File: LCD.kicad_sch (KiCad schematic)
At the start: 9 parts, among them J1 AFC01-S40FCA-00, J2 AFC07-S10ECC-00

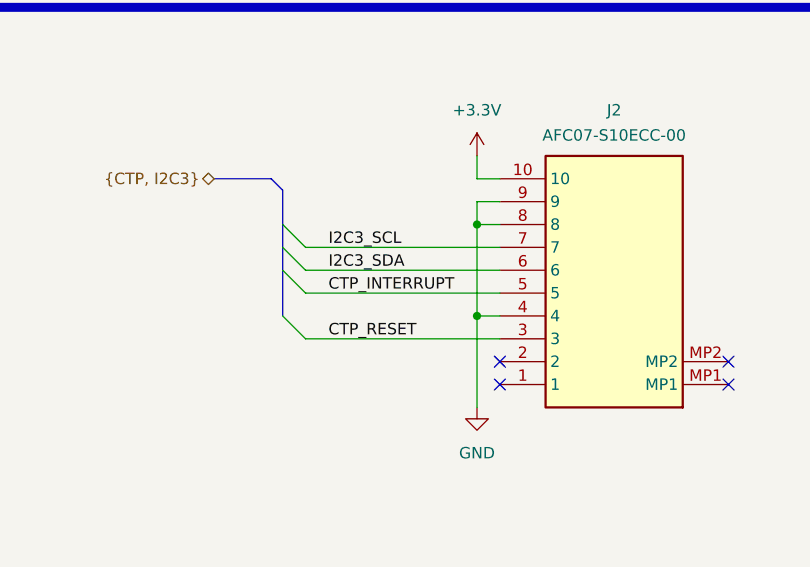
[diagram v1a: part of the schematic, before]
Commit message: added RF ransceiver
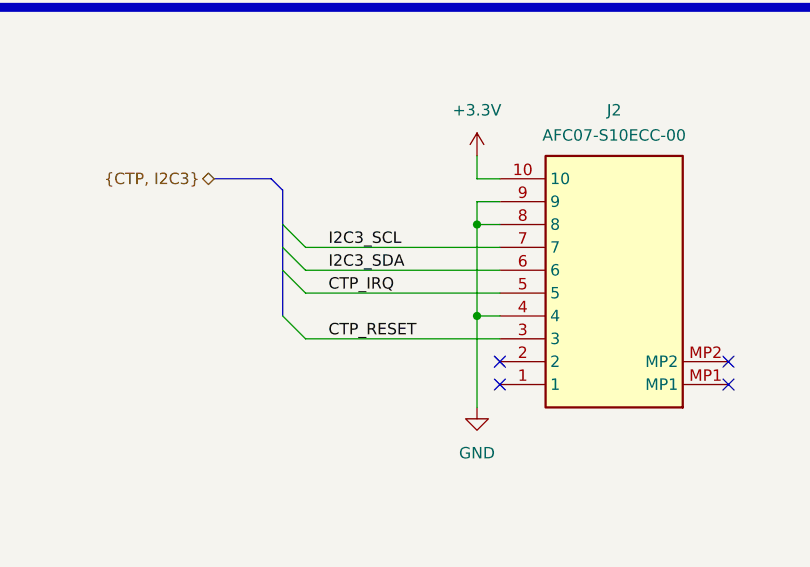
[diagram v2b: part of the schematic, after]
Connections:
- net CTP_INTERRUPT: no longer J2.5
- new net CTP_IRQ: J2.5
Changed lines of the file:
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@@
 	)
 	(bus_alias "CTP"
-		(members "CTP_INTERRUPT" "CTP_RESET")
+		(members "CTP_IRQ" "CTP_RESET")
 	)
 	(bus_alias "LCD_BACKLIGHT"
@@
 		)
 	)
-	(label "CTP_INTERRUPT"
+	(label "CTP_IRQ"
 		(at 227.33 198.12 0)
 		(effects

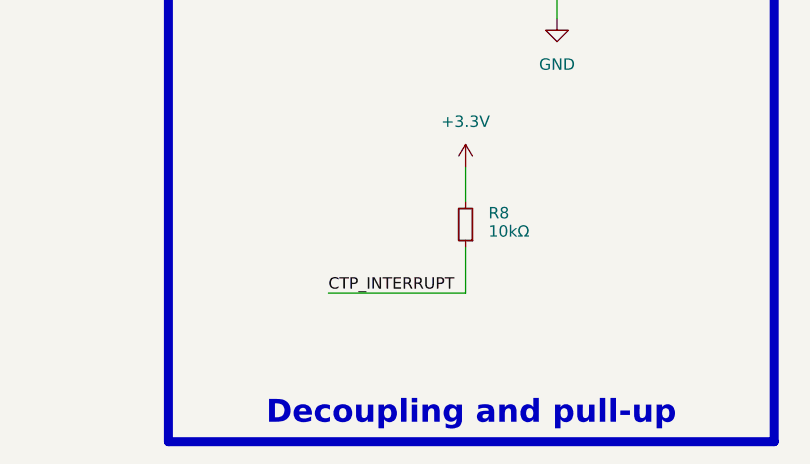
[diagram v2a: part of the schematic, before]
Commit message: added auxialry - swd connector and NRST pin circuit
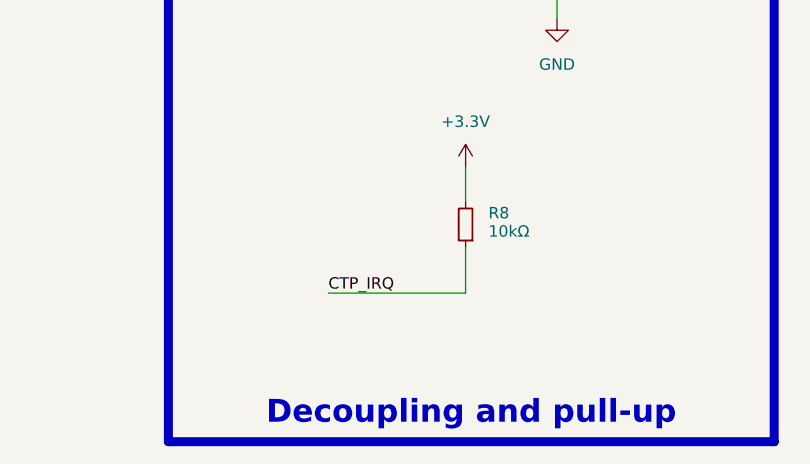
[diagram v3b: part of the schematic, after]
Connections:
- net CTP_INTERRUPT is gone; now on net CTP_IRQ: R8.1
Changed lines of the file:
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@@
-		)
-	)
-	(label "CTP_INTERRUPT"
-		(at 119.38 224.79 0)
-		(effects
-			(font
-				(size 1.27 1.27)
-			)
-			(justify left bottom)
 		)
 	)
@@
 		(effects
 			(font
+				(size 1.27 1.27)
+			)
+			(justify left bottom)
+		)
+	)
+	(label "CTP_IRQ"
+		(at 119.38 224.79 0)
+		(effects
+			(font

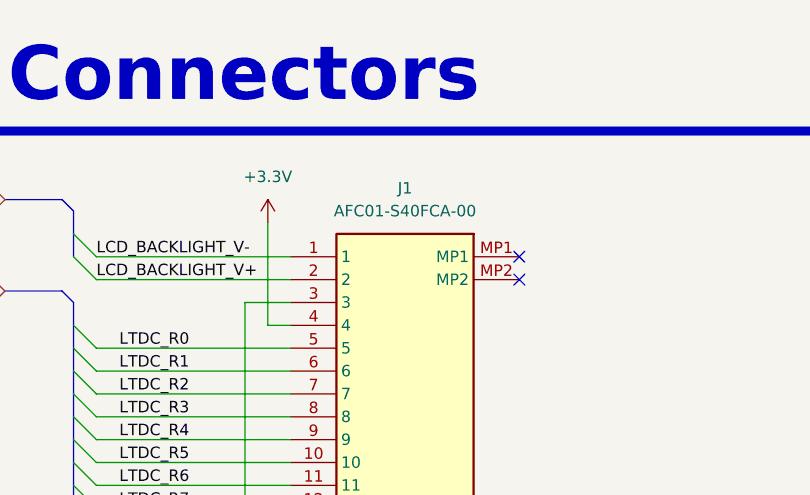
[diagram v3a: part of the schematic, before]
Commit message: routing zasilaczy + layout przetwornicy backlight, zmiana gniazd lcd connector - obrocenie top/bottom contacts, zmniejszenie gabarytow plytki - 100 height, przygotowanie pod 100width - max 100x100
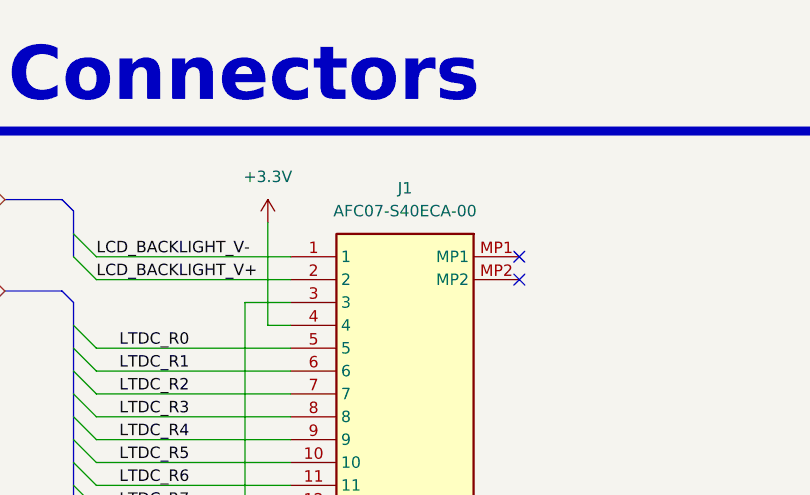
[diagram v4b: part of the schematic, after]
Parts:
- removed J1: AFC01-S40FCA-00, AFC01S40FCA00, symbol 0_connectors:AFC01-S40FCA-00
- added J1: AFC07-S40ECA-00, 0_connectors:AFC07-S40ECA-00, symbol 0_connectors:AFC07-S40ECA-00
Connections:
- net +3.3V: now also J1.4
- net GND: now also J1.29, J1.3, J1.36
- net LCD_BACKLIGHT_V+: now also J1.2
- net LCD_BACKLIGHT_V-: now also J1.1
- net LCD_DISP: now also J1.31
- net LTDC_B0: now also J1.21
- net LTDC_B1: now also J1.22
- net LTDC_B2: now also J1.23
- net LTDC_B3: now also J1.24
- net LTDC_B4: now also J1.25
- net LTDC_B5: now also J1.26
- net LTDC_B6: now also J1.27
- net LTDC_B7: now also J1.28
- net LTDC_CLK: now also J1.30
- net LTDC_DE: now also J1.34
- net LTDC_G0: now also J1.13
- net LTDC_G1: now also J1.14
- net LTDC_G2: now also J1.15
- net LTDC_G3: now also J1.16
- net LTDC_G4: now also J1.17
- net LTDC_G5: now also J1.18
- net LTDC_G6: now also J1.19
- net LTDC_G7: now also J1.20
- net LTDC_HSYNC: now also J1.32
- net LTDC_R0: now also J1.5
- net LTDC_R1: now also J1.6
- net LTDC_R2: now also J1.7
- net LTDC_R3: now also J1.8
- net LTDC_R4: now also J1.9
- net LTDC_R5: now also J1.10
- net LTDC_R6: now also J1.11
- net LTDC_R7: now also J1.12
- net LTDC_VSYNC: now also J1.33
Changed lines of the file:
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@@
-	)
-	(symbol
-		(lib_id "0_connectors:AFC01-S40FCA-00")
-		(at 271.78 39.37 0)
-		(mirror y)
-		(unit 1)
-		(exclude_from_sim no)
-		(in_bom yes)
-		(on_board yes)
-		(dnp no)
-		(fields_autoplaced yes)
-		(property "Reference" "J1"
-			(at 259.08 31.75 0)
-			(effects
-				(font
-					(size 1.27 1.27)
-				)
-			)
-		)
-		(property "Value" "AFC01-S40FCA-00"
-			(at 259.08 34.29 0)
-			(effects
-				(font
-					(size 1.27 1.27)
-				)
-			)
-		)
-		(property "Footprint" "AFC01S40FCA00"
-			(at 250.19 134.29 0)
-			(effects
-				(font
-					(size 1.27 1.27)
-				)
-				(justify left top)
-				(hide yes)
-			)
-		)
-		(property "Datasheet" "https://datasheet.lcsc.com/szlcsc/JUSHUO-AFC01-S40FCA-00_C262674.pdf"
-			(at 250.19 234.29 0)
-			(effects
-				(font
-					(size 1.27 1.27)
-				)
-				(justify left top)
-				(hide yes)
-			)
-		)
-		(property "Description" "FFC, FPC Connectors 0.020\"0.50mm P=0.5mm RoHS"
-			(at 271.78 39.37 0)
-			(effects
-				(font
-					(size 1.27 1.27)
-				)
-				(hide yes)
-			)
-		)
-		(property "Height" "3.6"
-			(at 250.19 434.29 0)
-			(effects
-				(font
-					(size 1.27 1.27)
-				)
-				(justify left top)
-				(hide yes)
-			)
-		)
-		(property "Manufacturer_Name" "JUSHUO"
-			(at 250.19 534.29 0)
-			(effects
-				(font
-					(size 1.27 1.27)
-				)
-				(justify left top)
-				(hide yes)
-			)
-		)
-		(property "Manufacturer_Part_Number" "AFC01-S40FCA-00"
-			(at 250.19 634.29 0)
-			(effects
-				(font
-					(size 1.27 1.27)
-				)
-				(justify left top)
-				(hide yes)
-			)
-		)
-		(property "Mouser Part Number" ""
-			(at 250.19 734.29 0)
-			(effects
-				(font
-					(size 1.27 1.27)
-				)
-				(justify left top)
-				(hide yes)
-			)
-		)
-		(property "Mouser Price/Stock" ""
-			(at 250.19 834.29 0)
-			(effects
-				(font
-					(size 1.27 1.27)
-				)
-				(justify left top)
-				(hide yes)
-			)
-		)
-		(property "Arrow Part Number" ""
-			(at 250.19 934.29 0)
-			(effects
-				(font
-					(size 1.27 1.27)
-				)
-				(justify left top)
-				(hide yes)
-			)
-		)
-		(property "Arrow Price/Stock" ""
-			(at 250.19 1034.29 0)
-			(effects
-				(font
-					(size 1.27 1.27)
-				)
-				(justify left top)
-				(hide yes)
-			)
-		)
-		(property "Supplier 1" "JLCPCB"
-			(at 271.78 39.37 0)
-			(effects
-				(font
-					(size 1.27 1.27)
-				)
-				(hide yes)
-			)
-		)
-		(property "Supplier Part Number 1" "C262674"
-			(at 271.78 39.37 0)
-			(effects
-				(font
-					(size 1.27 1.27)
-				)
-				(hide yes)
-			)
-		)
-		(pin "14"
-		)
-		(pin "34"
-		)
-		(pin "MP2"
-		)
-		(pin "29"
-		)
-		(pin "38"
-		)
-		(pin "13"
-		)
-		(pin "3"
-		)
-		(pin "16"
-		)
-		(pin "24"
-		)
-		(pin "36"
-		)
-		(pin "2"
-		)
-		(pin "21"
-		)
-		(pin "26"
-		)
-		(pin "15"
-		)
-		(pin "25"
-		)
-		(pin "31"
-		)
-		(pin "17"
-		)
-		(pin "9"
-		)
-		(pin "6"
-		)
-		(pin "12"
-		)
-		(pin "4"
-		)
-		(pin "18"
-		)
-		(pin "22"
-		)
-		(pin "10"
-		)
-		(pin "28"
-		)
-		(pin "5"
-		)
-		(pin "23"
-		)
-		(pin "27"
-		)
-		(pin "32"
-		)
-		(pin "33"
-		)
-		(pin "7"
-		)
-		(pin "MP1"
-		)
-		(pin "8"
-		)
-		(pin "11"
-		)
-		(pin "1"
-		)
-		(pin "19"
-		)
-		(pin "20"
-		)
-		(pin "30"
-		)
-		(pin "37"
-		)
-		(pin "39"
-		)
-		(pin "35"
-		)
-		(pin "40"
-		)
-		(instances
-			(project ""
-				(path "/0650c7a8-acba-429c-9f8e-eec0baf0bc1c/fede4c36-00cc-4d3d-b71c-5243ba232202/5eacbcca-1b40-44c5-850e-98771545fbe2"
-					(reference "J1")
-					(unit 1)
-				)
-			)
-		)
 	)
 	(symbol
@@
 					(unit 1)
 				)
+			)
+		)
+	)
+	(symbol
+		(lib_id "0_connectors:AFC07-S40ECA-00")
+		(at 271.78 39.37 0)
+		(mirror y)
+		(unit 1)
+		(exclude_from_sim no)
+		(in_bom yes)
+		(on_board yes)
+		(dnp no)
+		(property "Reference" "J1"
+			(at 259.08 31.75 0)
+			(effects
+				(font
+					(size 1.27 1.27)
+				)
+			)
+		)
+		(property "Value" "AFC07-S40ECA-00"
+			(at 259.08 34.29 0)
+			(effects
+				(font
+					(size 1.27 1.27)
+				)
+			)
+		)
+		(property "Footprint" "0_connectors:AFC07-S40ECA-00"
+			(at 250.19 134.29 0)
+			(effects
+				(font
+					(size 1.27 1.27)
+				)
+				(justify left top)
+				(hide yes)
+			)
+		)
+		(property "Datasheet" ""
+			(at 250.19 234.29 0)
+			(effects
+				(font
+					(size 1.27 1.27)
+				)
+				(justify left top)
+				(hide yes)
+			)
+		)
+		(property "Description" "FFC, FPC Connectors 0.020\"0.50mm P=0.5mm RoHS"
+			(at 271.78 39.37 0)
+			(effects
+				(font
+					(size 1.27 1.27)
+				)
+				(hide yes)
+			)
+		)
+		(property "Height" "3.6"
+			(at 250.19 434.29 0)
+			(effects
+				(font
+					(size 1.27 1.27)
+				)
+				(justify left top)
+				(hide yes)
+			)
+		)
+		(property "Manufacturer_Name" "JUSHUO"
+			(at 250.19 534.29 0)
+			(effects
+				(font
+					(size 1.27 1.27)
+				)
+				(justify left top)
+				(hide yes)
+			)
+		)
+		(property "Manufacturer_Part_Number" "AFC07-S40ECA-00 "
+			(at 250.19 634.29 0)
+			(effects
+				(font
+					(size 1.27 1.27)
+				)
+				(justify left top)
+				(hide yes)
+			)
+		)
+		(property "Mouser Part Number" ""
+			(at 250.19 734.29 0)
+			(effects
+				(font
+					(size 1.27 1.27)
+				)
+				(justify left top)
+				(hide yes)
+			)
+		)
+		(property "Mouser Price/Stock" ""
+			(at 250.19 834.29 0)
+			(effects
+				(font
+					(size 1.27 1.27)
+				)
+				(justify left top)
+				(hide yes)
+			)
+		)
+		(property "Arrow Part Number" ""
+			(at 250.19 934.29 0)
+			(effects
+				(font
+					(size 1.27 1.27)
+				)
+				(justify left top)
+				(hide yes)
+			)
+		)
+		(property "Arrow Price/Stock" ""
+			(at 250.19 1034.29 0)
+			(effects
+				(font
+					(size 1.27 1.27)
+				)
+				(justify left top)
+				(hide yes)
+			)
+		)
+		(property "Supplier 1" "JLCPCB"
+			(at 271.78 39.37 0)
+			(effects
+				(font
+					(size 1.27 1.27)
+				)
+				(hide yes)
+			)
+		)
+		(property "Supplier Part Number 1" "C262648"
+			(at 271.78 39.37 0)
+			(effects
+				(font
+					(size 1.27 1.27)
+				)
+				(hide yes)
+			)
+		)
+		(pin "14"
+		)
+		(pin "17"
+		)
+		(pin "3"
+		)
+		(pin "4"
+		)
+		(pin "7"
+		)
+		(pin "8"
+		)
+		(pin "10"
+		)
+		(pin "1"
+		)
+		(pin "MP1"
+		)
+		(pin "2"
+		)
+		(pin "6"
+		)
+		(pin "9"
+		)
+		(pin "MP2"
+		)
+		(pin "5"
+		)
+		(pin "11"
+		)
+		(pin "12"
+		)
+		(pin "13"
+		)
+		(pin "15"
+		)
+		(pin "16"
+		)
+		(pin "18"
+		)
+		(pin "19"
+		)
+		(pin "20"
+		)
+		(pin "30"
+		)
+		(pin "40"
+		)
+		(pin "21"
+		)
+		(pin "22"
+		)
+		(pin "36"
+		)
+		(pin "37"
+		)
+		(pin "27"
+		)
+		(pin "24"
+		)
+		(pin "39"
+		)
+		(pin "32"
+		)
+		(pin "33"
+		)
+		(pin "25"
+		)
+		(pin "29"
+		)
+		(pin "28"
+		)
+		(pin "31"
+		)
+		(pin "26"
+		)
+		(pin "23"
+		)
+		(pin "34"
+		)
+		(pin "35"
+		)
+		(pin "38"
+		)
+		(instances
+			(project ""
+				(path "/0650c7a8-acba-429c-9f8e-eec0baf0bc1c/fede4c36-00cc-4d3d-b71c-5243ba232202/5eacbcca-1b40-44c5-850e-98771545fbe2"
+					(reference "J1")
+					(unit 1)
+				)
